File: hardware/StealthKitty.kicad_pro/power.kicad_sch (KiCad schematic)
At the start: 27 parts, among them IC2 MP1475DJ-LF-P, SW3 Switch

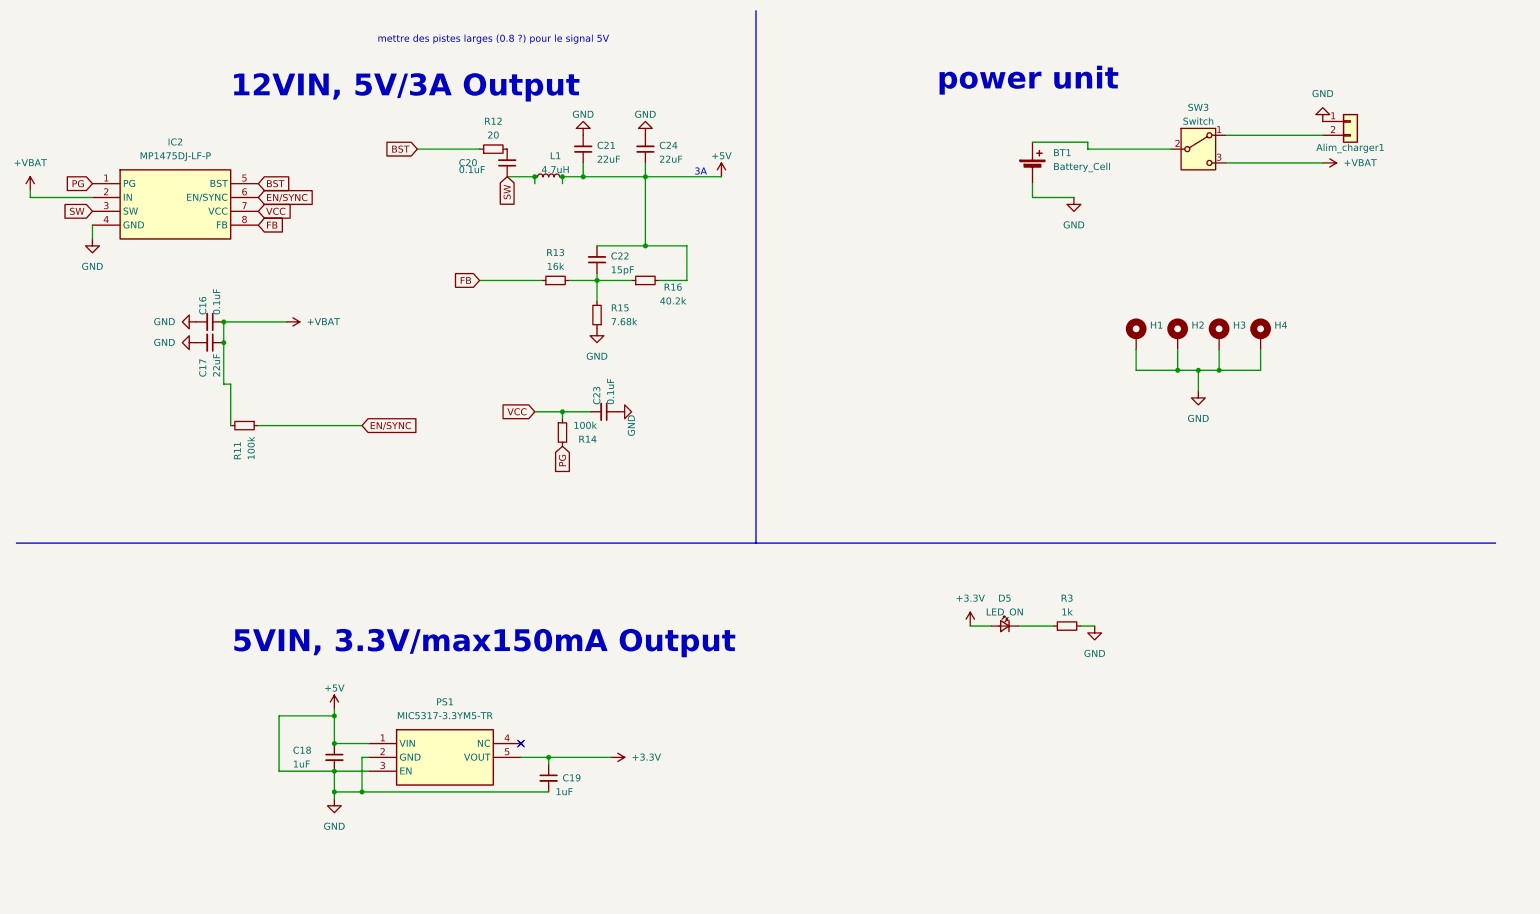
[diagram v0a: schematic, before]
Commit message: réassignation pins stm32, ajout des modifs de la partie power, ajout des modfis de la revue de projet 02/10/24, modifs du 3/10/24 voir readme
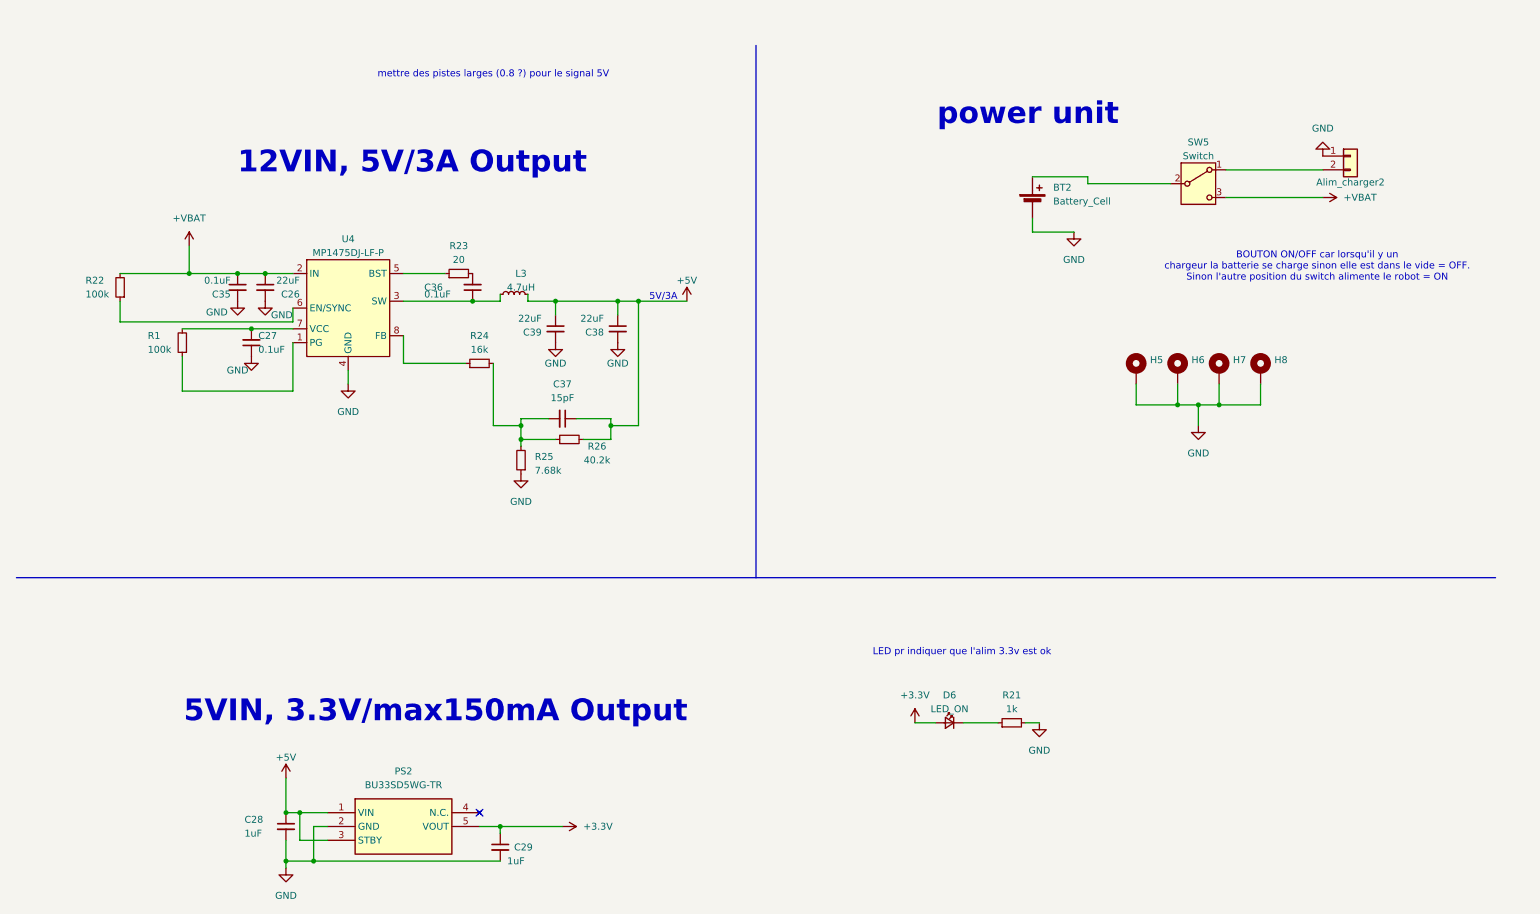
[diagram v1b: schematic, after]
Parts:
- removed Alim_charger1: Conn_01x02, Connector_JST:JST_XH_S2B-XH-A-1_1x02_P2.50mm_Horizontal, symbol Connector_Generic:Conn_01x02
- removed BT1: Battery_Cell, Connector_JST:JST_XH_S2B-XH-A-1_1x02_P2.50mm_Horizontal, symbol Device:Battery_Cell
- removed C16, C20, C23: 0.1uF, Capacitor_SMD:C_0603_1608Metric_Pad1.08x0.95mm_HandSolder, symbol Device:C_Small
- removed C17, C21, C24: 22uF, Capacitor_SMD:C_0603_1608Metric_Pad1.08x0.95mm_HandSolder, symbol Device:C_Small
- removed C18, C19: 1uF, Capacitor_SMD:C_0603_1608Metric_Pad1.08x0.95mm_HandSolder, symbol Device:C_Small
- removed C22: 15pF, Capacitor_SMD:C_0603_1608Metric_Pad1.08x0.95mm_HandSolder, symbol Device:C_Small
- removed D5: LED_ON, LED_SMD:LED_0603_1608Metric_Pad1.05x0.95mm_HandSolder, symbol Device:LED_Small
- removed H1, H2, H3, H4: ~, symbol Mechanical:MountingHole_Pad
- removed IC2: MP1475DJ-LF-P, SOT65P280X100-8N, symbol MP1475DJ-LF-P:MP1475DJ-LF-P
- removed L1: 4.7uH, Library:INDPM4141X210N, symbol Device:L_Small
- removed PS1: MIC5317-3.3YM5-TR, SOT95P280X145-5N, symbol MIC5317-3_3YM5-TR:MIC5317-3.3YM5-TR
- removed R11, R14: 100k, Resistor_SMD:R_0603_1608Metric_Pad0.98x0.95mm_HandSolder, symbol Device:R_Small
- removed R12: 20, Resistor_SMD:R_0805_2012Metric_Pad1.20x1.40mm_HandSolder, symbol Device:R_Small
- removed R13: 16k, Resistor_SMD:R_0603_1608Metric_Pad0.98x0.95mm_HandSolder, symbol Device:R_Small
- removed R15: 7.68k, Resistor_SMD:R_0603_1608Metric_Pad0.98x0.95mm_HandSolder, symbol Device:R_Small
- removed R16: 40.2k, Resistor_SMD:R_0603_1608Metric_Pad0.98x0.95mm_HandSolder, symbol Device:R_Small
- removed R3: 1k, Resistor_SMD:R_0603_1608Metric_Pad0.98x0.95mm_HandSolder, symbol Device:R_Small
- removed SW3: Switch, Connector_JST:JST_XH_S3B-XH-A_1x03_P2.50mm_Horizontal, symbol Switch:SW_SPDT
- added Alim_charger2: Conn_01x02, Connector_JST:JST_XH_S2B-XH-A-1_1x02_P2.50mm_Horizontal, symbol Connector_Generic:Conn_01x02
- added BT2: Battery_Cell, Connector_JST:JST_XH_S2B-XH-A-1_1x02_P2.50mm_Horizontal, symbol Device:Battery_Cell
- added C26, C38, C39: 22uF, Capacitor_SMD:C_0603_1608Metric_Pad1.08x0.95mm_HandSolder, symbol Device:C_Small
- added C27, C35, C36: 0.1uF, Capacitor_SMD:C_0603_1608Metric_Pad1.08x0.95mm_HandSolder, symbol Device:C_Small
- added C28, C29: 1uF, Capacitor_SMD:C_0603_1608Metric_Pad1.08x0.95mm_HandSolder, symbol Device:C_Small
- added C37: 15pF, Capacitor_SMD:C_0603_1608Metric_Pad1.08x0.95mm_HandSolder, symbol Device:C_Small
- added D6: LED_ON, LED_SMD:LED_0603_1608Metric_Pad1.05x0.95mm_HandSolder, symbol Device:LED_Small
- added H5, H6, H7, H8: ~, symbol Mechanical:MountingHole_Pad
- added L3: 4.7uH, Library:INDPM4141X210N, symbol Device:L_Small
- added PS2: BU33SD5WG-TR, SOT95P280X125-5N, symbol BU33SD5WG-TR:BU33SD5WG-TR
- added R1, R22: 100k, Resistor_SMD:R_0603_1608Metric_Pad0.98x0.95mm_HandSolder, symbol Device:R_Small
- added R21: 1k, Resistor_SMD:R_0603_1608Metric_Pad0.98x0.95mm_HandSolder, symbol Device:R_Small
- added R23: 20, Resistor_SMD:R_0805_2012Metric_Pad1.20x1.40mm_HandSolder, symbol Device:R_Small
- added R24: 16k, Resistor_SMD:R_0603_1608Metric_Pad0.98x0.95mm_HandSolder, symbol Device:R_Small
- added R25: 7.68k, Resistor_SMD:R_0603_1608Metric_Pad0.98x0.95mm_HandSolder, symbol Device:R_Small
- added R26: 40.2k, Resistor_SMD:R_0603_1608Metric_Pad0.98x0.95mm_HandSolder, symbol Device:R_Small
- added SW5: Switch, Connector_JST:JST_XH_S3B-XH-A_1x03_P2.50mm_Horizontal, symbol Switch:SW_SPDT
- added U4: MP1475DJ-LF-P, Library:SOT65P280X100-8N, symbol Ludzlib:MP1475
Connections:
- net +3.3V: now also C29.1, D6.2 (A), PS2.5 (VOUT)
- net +5V: now also C28.1, C37.1, C38.1, C39.1, L3.2, PS2.1 (VIN), PS2.3 (STBY), R26.2
- net +VBAT: now also C26.1, C35.1, R22.2, SW5.3 (C), U4.2 (IN)
- new net: C37.2, R24.2, R25.2, R26.1
- new net: R22.1, U4.6 (EN/SYNC)
- new net: C36.1, L3.1, U4.3 (SW)
- new net: C27.2, R1.2, U4.7 (VCC)
- new net: R23.1, U4.5 (BST)
- new net: C36.2, R23.2
- new net: R1.1, U4.1 (PG)
- new net: R24.1, U4.8 (FB)
- new net: BT2.1 (+), SW5.2 (B)
- new net: Alim_charger2.2 (Pin_2), SW5.1 (A)
- new net: D6.1 (K), R21.1
- new net GND: Alim_charger2.1 (Pin_1), BT2.2 (-), C26.2, C27.1, C28.2, C29.2, C35.2, C38.2, C39.2, H5.1, H6.1, H7.1, H8.1, PS2.2 (GND), R21.2, R25.1, U4.4 (GND)
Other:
- note added: "5V/3A"
- note added: "BOUTON ON/OFF car lorsqu'il y un chargeur la batterie se charge sinon elle est dans le vide = OFF. Sinon l'autre position du switch alimente le robot = ON"
- note added: "LED pr indiquer que l'alim 3.3v est ok"
- note removed: "3A"

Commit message: MAJ routage equipe
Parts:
- removed H5, H6, H7, H8: ~, symbol Mechanical:MountingHole_Pad
- C26, C38, C39: footprint Capacitor_SMD:C_0603_1608Metric_Pad1.08x0.95mm_HandSolder -> Capacitor_SMD:C_0805_2012Metric_Pad1.18x1.45mm_HandSolder
- C27, C35, C36, C37: footprint Capacitor_SMD:C_0603_1608Metric_Pad1.08x0.95mm_HandSolder -> Capacitor_SMD:C_0402_1005Metric_Pad0.74x0.62mm_HandSolder
- L3: footprint Library:INDPM4141X210N -> Library:INDPM5050X200N
- PS2: footprint SOT95P280X125-5N -> Library:SOT95P280X125-5N
- R23: footprint Resistor_SMD:R_0805_2012Metric_Pad1.20x1.40mm_HandSolder -> Resistor_SMD:R_0603_1608Metric_Pad0.98x0.95mm_HandSolder
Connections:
- no-connect marks 1 -> 0
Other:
- moved on the sheet: Alim_charger2, BT2

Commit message: Confirmation placement equipe
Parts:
- removed U4: MP1475DJ-LF-P, Library:SOT65P280X100-8N, symbol Ludzlib:MP1475
- added IC501: MP1475DJ-LF-P, Library:SOT65P280X100-8N, symbol MP1475DJ-LF-P:MP1475DJ-LF-P
- renumbered Alim_charger2 to Alim_charger501, BT2 to BT501, C35 to C501, C27 to C502, C26 to C503, C28 to C504, C36 to C505, C29 to C506, C39 to C507, C37 to C508, C38 to C509, D6 to D501, L3 to L501, PS2 to PS501, R22 to R501, R1 to R502, R23 to R503, R24 to R504, R25 to R505, R26 to R506, R21 to R507, SW5 to SW501
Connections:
- net +VBAT: now also IC501.2 (IN)
- net GND: now also IC501.4 (GND)
- net at R501.1: now also IC501.6 (EN/SYNC)
- net at C505.1, L501.1: now also IC501.3 (SW)
- net at C502.2, R502.2: now also IC501.7 (VCC)
- net at R503.1: now also IC501.5 (BST)
- net at R502.1: now also IC501.1 (PG)
- net at R504.1: now also IC501.8 (FB)
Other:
- moved on the sheet: C501, C502, C503, R501, R502

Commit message: Dernier Modif 08/10/2024
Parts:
- BT501: footprint Connector_JST:JST_XH_S2B-XH-A-1_1x02_P2.50mm_Horizontal -> Connector_JST:JST_XH_S2B-XH-A_1x02_P2.50mm_Horizontal
- C501: value 0.1uF -> 22uF; footprint Capacitor_SMD:C_0402_1005Metric_Pad0.74x0.62mm_HandSolder -> Capacitor_SMD:C_0402_1005Metric
- C502, C505, C508: footprint Capacitor_SMD:C_0402_1005Metric_Pad0.74x0.62mm_HandSolder -> Capacitor_SMD:C_0402_1005Metric
- C503: value 22uF -> 0.1uF; footprint Capacitor_SMD:C_0805_2012Metric_Pad1.18x1.45mm_HandSolder -> Capacitor_SMD:C_0402_1005Metric
- C504, C506: footprint Capacitor_SMD:C_0603_1608Metric_Pad1.08x0.95mm_HandSolder -> Capacitor_SMD:C_0402_1005Metric
- C507, C509: footprint Capacitor_SMD:C_0805_2012Metric_Pad1.18x1.45mm_HandSolder -> Capacitor_SMD:C_0402_1005Metric
- R501, R502, R503, R504, R505, R506, R507: footprint Resistor_SMD:R_0603_1608Metric_Pad0.98x0.95mm_HandSolder -> Resistor_SMD:R_0402_1005Metric
- SW501: footprint Connector_JST:JST_XH_S3B-XH-A_1x03_P2.50mm_Horizontal -> Connector_JST:JST_XH_S3B-XH-A-1_1x03_P2.50mm_Horizontal
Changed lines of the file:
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@@
 			)
 		)
-		(property "Footprint" "Resistor_SMD:R_0603_1608Metric_Pad0.98x0.95mm_HandSolder"
+		(property "Footprint" "Resistor_SMD:R_0402_1005Metric"
 			(at 114.3 91.44 0)
 			(effects
@@
 			)
 		)
-		(property "Footprint" "Resistor_SMD:R_0603_1608Metric_Pad0.98x0.95mm_HandSolder"
+		(property "Footprint" "Resistor_SMD:R_0402_1005Metric"
 			(at 25.4 63.5 0)
 			(effects
@@
 			)
 		)
-		(property "Value" "0.1uF"
+		(property "Value" "22uF"
 			(at 45.72 62.23 0)
 			(effects
@@
 			)
 		)
-		(property "Footprint" "Capacitor_SMD:C_0402_1005Metric_Pad0.74x0.62mm_HandSolder"
+		(property "Footprint" "Capacitor_SMD:C_0402_1005Metric"
 			(at 46.99 63.5 0)
 			(effects
@@
 			)
 		)
-		(property "Footprint" "Capacitor_SMD:C_0805_2012Metric_Pad1.18x1.45mm_HandSolder"
+		(property "Footprint" "Capacitor_SMD:C_0402_1005Metric"
 			(at 123.19 71.12 0)
 			(effects
@@
 			)
 		)
-		(property "Footprint" "Resistor_SMD:R_0603_1608Metric_Pad0.98x0.95mm_HandSolder"
+		(property "Footprint" "Resistor_SMD:R_0402_1005Metric"
 			(at 105.41 95.25 0)
 			(effects
@@
 			)
 		)
-		(property "Footprint" "Capacitor_SMD:C_0402_1005Metric_Pad0.74x0.62mm_HandSolder"
+		(property "Footprint" "Capacitor_SMD:C_0402_1005Metric"
 			(at 50.8 77.47 0)
 			(effects
@@
 			)
 		)
-		(property "Footprint" "Resistor_SMD:R_0603_1608Metric_Pad0.98x0.95mm_HandSolder"
+		(property "Footprint" "Resistor_SMD:R_0402_1005Metric"
 			(at 93.98 60.96 0)
 			(effects
@@
 			)
 		)
-		(property "Footprint" "Capacitor_SMD:C_0603_1608Metric_Pad1.08x0.95mm_HandSolder"
+		(property "Footprint" "Capacitor_SMD:C_0402_1005Metric"
 			(at 62.23 162.56 0)
 			(effects
@@
 			)
 		)
-		(property "Footprint" "Capacitor_SMD:C_0402_1005Metric_Pad0.74x0.62mm_HandSolder"
+		(property "Footprint" "Capacitor_SMD:C_0402_1005Metric"
 			(at 96.52 63.5 0)
 			(effects
@@
 			)
 		)
-		(property "Footprint" "Resistor_SMD:R_0603_1608Metric_Pad0.98x0.95mm_HandSolder"
+		(property "Footprint" "Resistor_SMD:R_0402_1005Metric"
 			(at 97.79 77.47 0)
 			(effects
@@
 			)
 		)
-		(property "Footprint" "Resistor_SMD:R_0603_1608Metric_Pad0.98x0.95mm_HandSolder"
+		(property "Footprint" "Resistor_SMD:R_0402_1005Metric"
 			(at 38.1 77.47 0)
 			(effects
@@
 			)
 		)
-		(property "Footprint" "Connector_JST:JST_XH_S2B-XH-A-1_1x02_P2.50mm_Horizontal"
+		(property "Footprint" "Connector_JST:JST_XH_S2B-XH-A_1x02_P2.50mm_Horizontal"
 			(at 210.82 48.006 90)
 			(effects
@@
 			)
 		)
-		(property "Footprint" "Connector_JST:JST_XH_S3B-XH-A_1x03_P2.50mm_Horizontal"
+		(property "Footprint" "Connector_JST:JST_XH_S3B-XH-A-1_1x03_P2.50mm_Horizontal"
 			(at 229.87 44.45 0)
 			(effects
@@
 			)
 		)
-		(property "Footprint" "Capacitor_SMD:C_0603_1608Metric_Pad1.08x0.95mm_HandSolder"
+		(property "Footprint" "Capacitor_SMD:C_0402_1005Metric"
 			(at 101.6 166.37 0)
 			(effects
@@
 			)
 		)
-		(property "Footprint" "Capacitor_SMD:C_0805_2012Metric_Pad1.18x1.45mm_HandSolder"
+		(property "Footprint" "Capacitor_SMD:C_0402_1005Metric"
 			(at 111.76 71.12 0)
 			(effects
@@
 			)
 		)
-		(property "Value" "22uF"
+		(property "Value" "0.1uF"
 			(at 58.42 62.23 0)
 			(effects
@@
 			)
 		)
-		(property "Footprint" "Capacitor_SMD:C_0805_2012Metric_Pad1.18x1.45mm_HandSolder"
+		(property "Footprint" "Capacitor_SMD:C_0402_1005Metric"
 			(at 52.07 63.5 0)
 			(effects
@@
 			)
 		)
-		(property "Footprint" "Capacitor_SMD:C_0402_1005Metric_Pad0.74x0.62mm_HandSolder"
+		(property "Footprint" "Capacitor_SMD:C_0402_1005Metric"
 			(at 113.03 87.63 0)
 			(effects
@@
 			)
 		)
-		(property "Footprint" "Resistor_SMD:R_0603_1608Metric_Pad0.98x0.95mm_HandSolder"
+		(property "Footprint" "Resistor_SMD:R_0402_1005Metric"
 			(at 195.58 143.51 0)
 			(effects

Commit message: Modification Placement 09/10/24
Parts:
- BT501: footprint Connector_JST:JST_XH_S2B-XH-A_1x02_P2.50mm_Horizontal -> Connector_JST:JST_XH_S2B-XH-A-1_1x02_P2.50mm_Horizontal
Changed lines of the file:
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@@
 			)
 		)
-		(property "Footprint" "Connector_JST:JST_XH_S2B-XH-A_1x02_P2.50mm_Horizontal"
+		(property "Footprint" "Connector_JST:JST_XH_S2B-XH-A-1_1x02_P2.50mm_Horizontal"
 			(at 210.82 48.006 90)
 			(effects
